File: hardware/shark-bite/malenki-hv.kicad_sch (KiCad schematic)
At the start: 18 parts, among them J1 Conn_01x02_Male-Connector, J2 Conn_01x08_Male, J3 Conn_01x02, U2 AP2204RA-3.3TRG1, U3 ATTiny1616-MNR

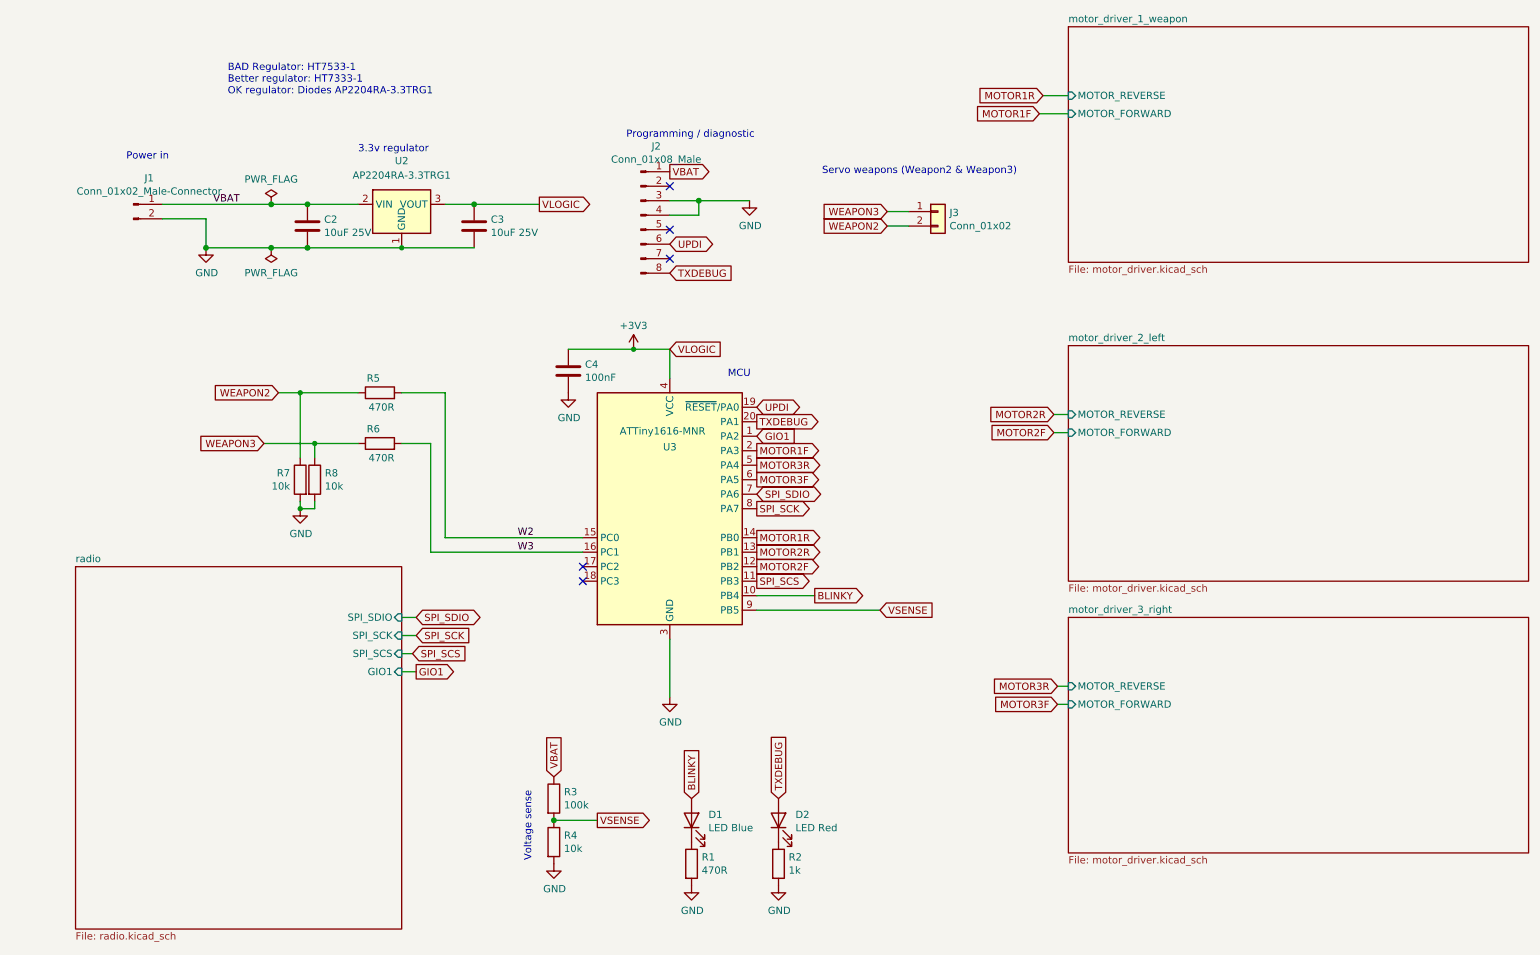
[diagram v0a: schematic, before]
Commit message: Added TVS Diodes
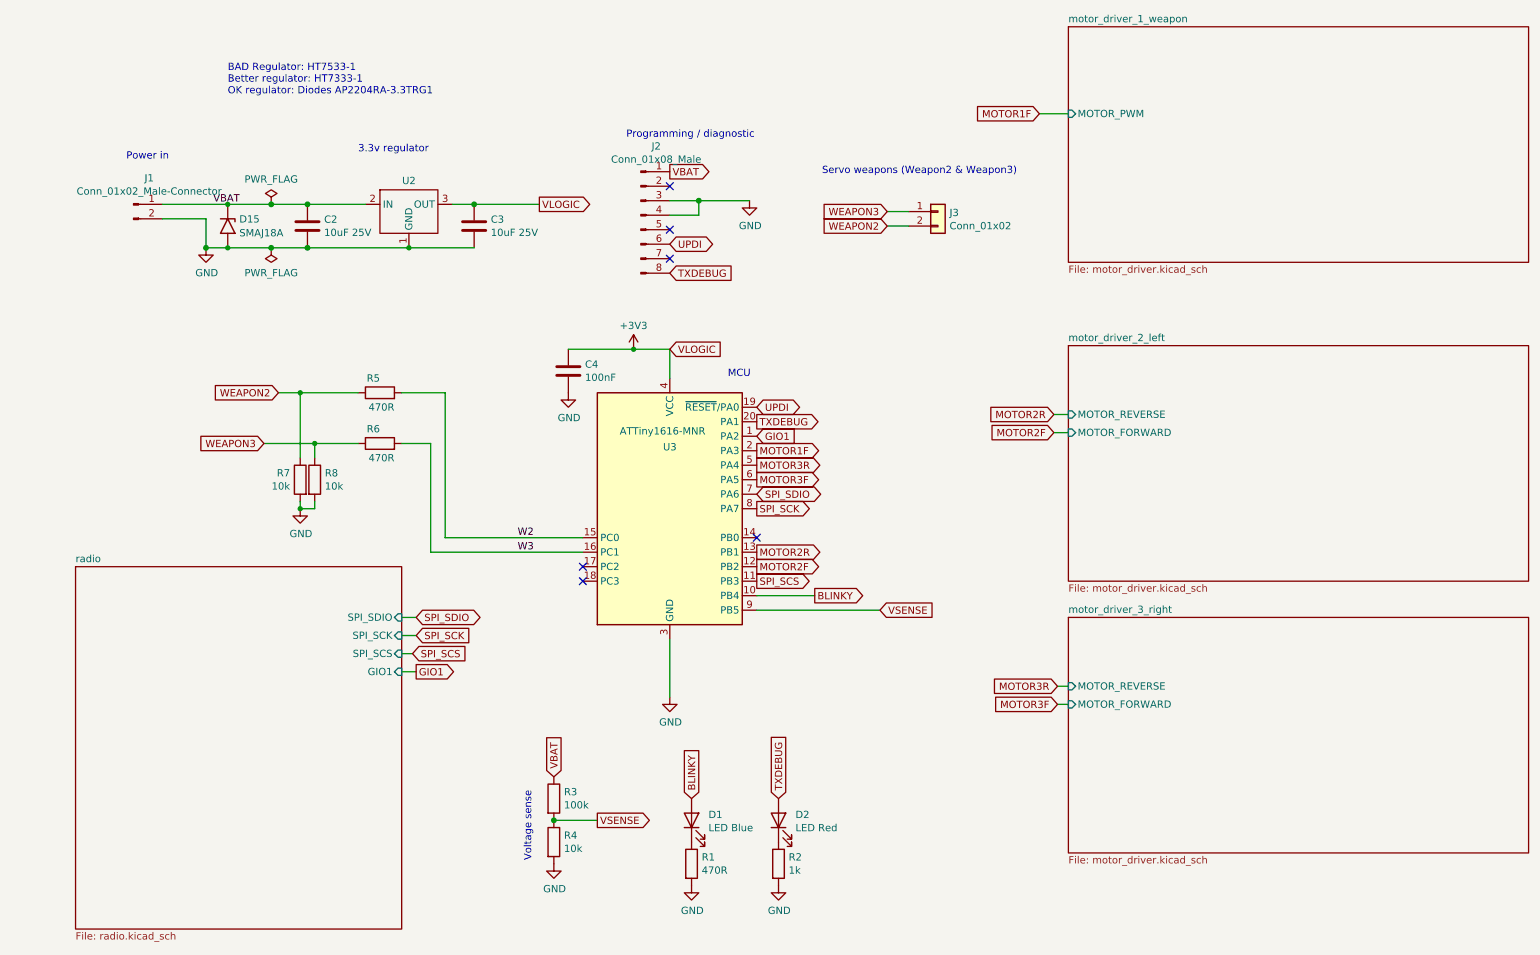
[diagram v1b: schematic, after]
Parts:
- removed U2: AP2204RA-3.3TRG1, Package_TO_SOT_SMD:SOT-89-3, symbol Regulator_Linear:HT75xx-1-SOT89
- added D15: SMAJ18A, Diode_SMD:D_SMA, symbol Diode:SMAJ18A
- added U2: ~, Package_TO_SOT_SMD:SOT-89-3, symbol Sharkbite:GATEMODE_GM7333
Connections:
- net +3V3: now also U2.3 (OUT)
- net GND: now also D15.2 (A2), U2.1 (GND)
- net VBAT: now also D15.1 (A1), U2.2 (IN)
- net MOTOR1R: no longer names the net of U3.14 (PB0)
- no-connect marks 5 -> 6
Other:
- sheet motor_driver_1_weapon ports: added MOTOR_PWM; removed MOTOR_FORWARD, MOTOR_REVERSE
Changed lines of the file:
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@@
   (junction (at 64.77 90.17) (diameter 0) (color 0 0 0 0)
   )
+  (junction (at 49.53 48.26) (diameter 0) (color 0 0 0 0)
+  )
   (junction (at 63.5 55.88) (diameter 1.016) (color 0 0 0 0)
   )
   (junction (at 92.71 48.26) (diameter 1.016) (color 0 0 0 0)
   )
+  (junction (at 81.28 55.88) (diameter 0) (color 0 0 0 0)
+  )
+  (junction (at 49.53 55.88) (diameter 0) (color 0 0 0 0)
+  )
   (junction (at 45.72 55.88) (diameter 1.016) (color 0 0 0 0)
   )
   (junction (at 62.23 81.28) (diameter 0) (color 0 0 0 0)
-  )
-  (junction (at 80.01 55.88) (diameter 0) (color 0 0 0 0)
   )
   (junction (at 57.15 48.26) (diameter 1.016) (color 0 0 0 0)
@@
   (no_connect (at 111.76 111.76))
   (no_connect (at 127 45.085))
+  (no_connect (at 142.24 106.68))
   (wire (pts (xy 165.1 52.07) (xy 168.91 52.07))
     (stroke (width 0) (type solid))
@@
     (stroke (width 0) (type default))
   )
-  (wire (pts (xy 38.1 48.26) (xy 57.15 48.26))
+  (wire (pts (xy 38.1 48.26) (xy 49.53 48.26))
+    (stroke (width 0) (type solid))
+  )
+  (wire (pts (xy 81.28 55.88) (xy 92.71 55.88))
     (stroke (width 0) (type solid))
   )
@@
     (stroke (width 0) (type solid))
   )
-  (wire (pts (xy 45.72 55.88) (xy 57.15 55.88))
+  (wire (pts (xy 45.72 55.88) (xy 49.53 55.88))
     (stroke (width 0) (type solid))
   )
@@
     (stroke (width 0) (type default))
   )
+  (wire (pts (xy 49.53 48.26) (xy 57.15 48.26))
+    (stroke (width 0) (type default))
+  )
   (wire (pts (xy 55.88 90.17) (xy 64.77 90.17))
     (stroke (width 0) (type default))
   )
-  (wire (pts (xy 80.01 55.88) (xy 92.71 55.88))
-    (stroke (width 0) (type solid))
-  )
   (wire (pts (xy 80.01 90.17) (xy 85.09 90.17))
     (stroke (width 0) (type default))
@@
     (stroke (width 0) (type default))
   )
-  (wire (pts (xy 63.5 55.88) (xy 80.01 55.88))
-    (stroke (width 0) (type solid))
-  )
   (wire (pts (xy 127 50.165) (xy 132.08 50.165))
     (stroke (width 0) (type solid))
@@
     (stroke (width 0) (type solid))
   )
-  (wire (pts (xy 63.5 48.26) (xy 72.39 48.26))
+  (wire (pts (xy 63.5 55.88) (xy 81.28 55.88))
+    (stroke (width 0) (type default))
+  )
+  (wire (pts (xy 63.5 48.26) (xy 73.66 48.26))
     (stroke (width 0) (type solid))
   )
@@
     (stroke (width 0) (type default))
   )
-  (wire (pts (xy 87.63 48.26) (xy 92.71 48.26))
-    (stroke (width 0) (type solid))
+  (wire (pts (xy 88.9 48.26) (xy 92.71 48.26))
+    (stroke (width 0) (type solid))
+  )
+  (wire (pts (xy 49.53 55.88) (xy 57.15 55.88))
+    (stroke (width 0) (type default))
   )
   (wire (pts (xy 62.23 81.28) (xy 62.23 92.71))
@@
   )
   (wire (pts (xy 165.1 49.53) (xy 168.91 49.53))
-    (stroke (width 0) (type solid))
-  )
-  (wire (pts (xy 192.405 29.21) (xy 196.85 29.21))
     (stroke (width 0) (type solid))
   )
@@
     (effects (font (size 1.27 1.27)) (justify right))
     (property "Intersheetrefs" "${INTERSHEET_REFS}" (at -53.34 -27.94 0)
-      (effects (font (size 1.27 1.27)) hide)
-    )
-  )
-  (global_label "MOTOR1R" (shape output) (at 142.24 106.68 0) (fields_autoplaced)
-    (effects (font (size 1.27 1.27)) (justify left))
-    (property "Intersheetrefs" "${INTERSHEET_REFS}" (at 154.0704 106.68 0)
-      (effects (font (size 1.27 1.27)) (justify left) hide)
-    )
-  )
-  (global_label "MOTOR1R" (shape input) (at 192.405 29.21 180)
-    (effects (font (size 1.27 1.27)) (justify right))
-    (property "Intersheetrefs" "${INTERSHEET_REFS}" (at 334.645 135.89 0)
       (effects (font (size 1.27 1.27)) hide)
     )
@@
         (path "/f41619e3-8cf2-4511-8a51-762d4de43197"
           (reference "D2") (unit 1)
+        )
+      )
+    )
+  )
+  (symbol (lib_id "Diode:SMAJ18A") (at 49.53 52.07 270) (unit 1)
+    (in_bom yes) (on_board yes) (dnp no) (fields_autoplaced)
+    (property "Reference" "D15" (at 51.562 50.8579 90)
+      (effects (font (size 1.27 1.27)) (justify left))
+    )
+    (property "Value" "SMAJ18A" (at 51.562 53.2821 90)
+      (effects (font (size 1.27 1.27)) (justify left))
+    )
+    (property "Footprint" "Diode_SMD:D_SMA" (at 44.45 52.07 0)
+      (effects (font (size 1.27 1.27)) hide)
+    )
+    (property "Datasheet" "https://www.littelfuse.com/media?resourcetype=datasheets&itemid=75e32973-b177-4ee3-a0ff-cedaf1abdb93&filename=smaj-datasheet" (at 49.53 50.8 0)
+      (effects (font (size 1.27 1.27)) hide)
+    )
+    (pin "1")
+    (pin "2")
+    (instances
+      (project "malenki-hv"
+        (path "/f41619e3-8cf2-4511-8a51-762d4de43197/b339fba4-a8e4-4c66-ad9c-610bd968ae93"
+          (reference "D15") (unit 1)
+        )
+        (path "/f41619e3-8cf2-4511-8a51-762d4de43197/159e78dd-19f3-45d1-a83d-5b1f96539c1f"
+          (reference "D16") (unit 1)
+        )
+        (path "/f41619e3-8cf2-4511-8a51-762d4de43197/ed035ea4-687d-4ec6-a6e6-057c20ae2a22"
+          (reference "D17") (unit 1)
+        )
+        (path "/f41619e3-8cf2-4511-8a51-762d4de43197"
+          (reference "D18") (unit 1)
         )
       )
@@
         (path "/f41619e3-8cf2-4511-8a51-762d4de43197"
           (reference "R6") (unit 1)
+        )
+      )
+    )
+  )
+  (symbol (lib_id "Sharkbite:GATEMODE_GM7333") (at 81.28 48.26 0) (unit 1)
+    (in_bom yes) (on_board yes) (dnp no) (fields_autoplaced)
+    (property "Reference" "U2" (at 81.28 44.1269 0)
+      (effects (font (size 1.27 1.27)))
+    )
+    (property "Value" "~" (at 80.01 45.72 0)
+      (effects (font (size 1.27 1.27)))
+    )
+    (property "Footprint" "Package_TO_SOT_SMD:SOT-89-3" (at 80.01 45.72 0)
+      (effects (font (size 1.27 1.27)) hide)
+    )
+    (property "Datasheet" "https://www.lcsc.com/datasheet/lcsc_datasheet_2308181508_GATEMODE-GM7333_C2833582.pdf" (at 80.01 45.72 0)
+      (effects (font (size 1.27 1.27)) hide)
+    )
+    (pin "1")
+    (pin "2")
+    (pin "3")
+    (instances
+      (project "malenki-hv"
+        (path "/f41619e3-8cf2-4511-8a51-762d4de43197"
+          (reference "U2") (unit 1)
         )
       )
@@
     )
   )
-  (symbol (lib_id "Regulator_Linear:HT75xx-1-SOT89") (at 80.01 50.8 0) (unit 1)
-    (in_bom yes) (on_board yes) (dnp no) (fields_autoplaced)
-    (property "Reference" "U2" (at 80.01 40.64 0)
-      (effects (font (size 1.27 1.27)))
-    )
-    (property "Value" "AP2204RA-3.3TRG1" (at 80.01 43.18 0)
-      (effects (font (size 1.27 1.27)))
-    )
-    (property "Footprint" "Package_TO_SOT_SMD:SOT-89-3" (at 80.01 42.545 0)
-      (effects (font (size 1.27 1.27) italic) hide)
-    )
-    (property "Datasheet" "" (at 80.01 48.26 0)
-      (effects (font (size 1.27 1.27)) hide)
-    )
-    (property "LCSC" "C151625" (at 80.01 50.8 0)
-      (effects (font (size 1.27 1.27)) hide)
-    )
-    (property "Manufacturer" "Diodes" (at 80.01 50.8 0)
-      (effects (font (size 1.27 1.27)) hide)
-    )
-    (pin "1")
-    (pin "2")
-    (pin "3")
-    (instances
-      (project "malenki-hv"
-        (path "/f41619e3-8cf2-4511-8a51-762d4de43197"
-          (reference "U2") (unit 1)
-        )
-      )
-    )
-  )
   (symbol (lib_id "malenki-nano-rescue:PWR_FLAG-power") (at 57.15 55.88 180) (unit 1)
     (in_bom yes) (on_board yes) (dnp no)
@@
       (effects (font (size 1.27 1.27)) (justify left top))
     )
-    (pin "MOTOR_REVERSE" input (at 196.85 29.21 180)
-      (effects (font (size 1.27 1.27)) (justify left))
-    )
-    (pin "MOTOR_FORWARD" input (at 196.85 32.385 180)
-      (effects (font (size 1.27 1.27)) (justify left))
-    )
+    (pin "MOTOR_PWM" input (at 196.85 32.385 180)
+      (effects (font (size 1.27 1.27)) (justify left))
+    )

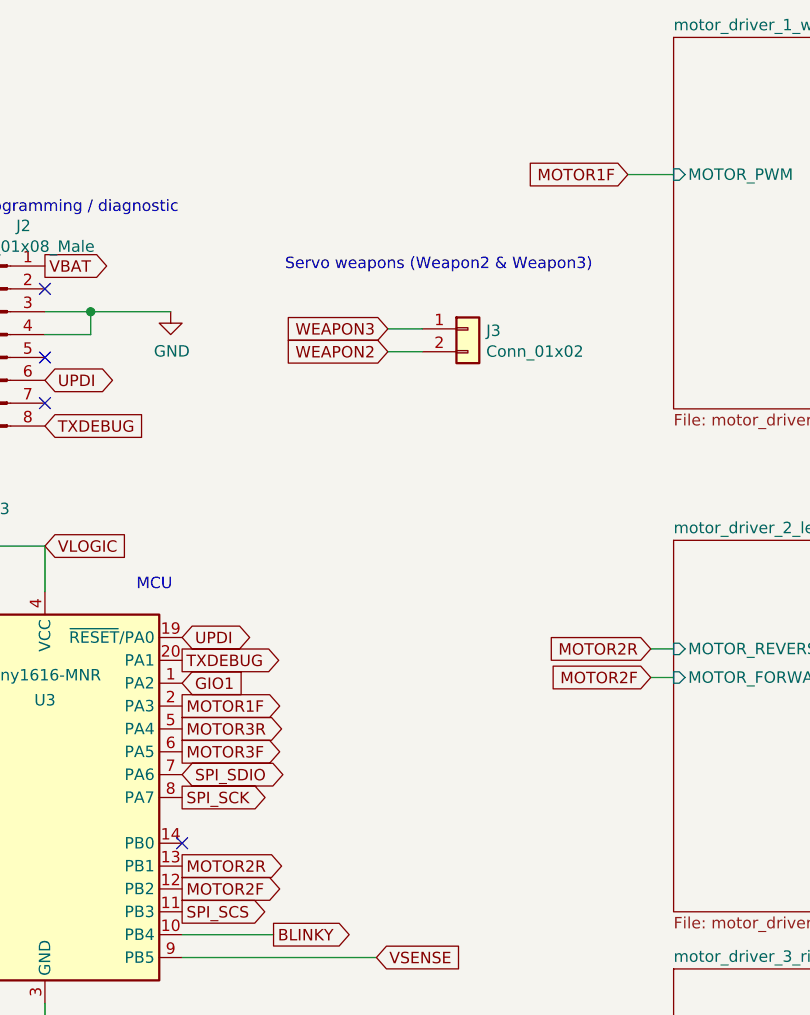
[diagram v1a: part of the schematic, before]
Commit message: Removed Extra Diodes
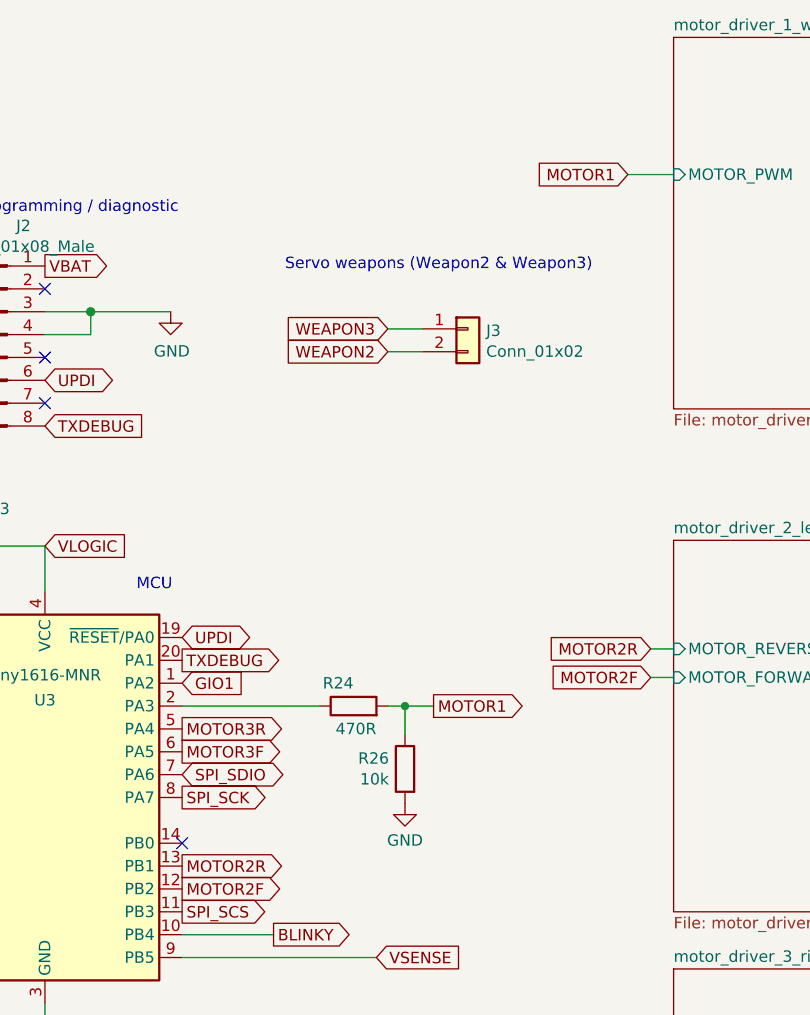
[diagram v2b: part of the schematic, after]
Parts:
- added R24: 470R, Resistor_SMD:R_0402_1005Metric, symbol malenki-nano-rescue:R-Device
- added R26: 10k, Resistor_SMD:R_0402_1005Metric, symbol malenki-nano-rescue:R-Device
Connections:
- net GND: now also R26.2
- net MOTOR1F: no longer names the net of U3.2 (PA3)
- net MOTOR1F: now also R24.1
- new net MOTOR1: R24.2, R26.1
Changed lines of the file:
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@@
   (junction (at 45.72 55.88) (diameter 1.016) (color 0 0 0 0)
+  )
+  (junction (at 167.005 91.44) (diameter 0) (color 0 0 0 0)
   )
   (junction (at 62.23 81.28) (diameter 0) (color 0 0 0 0)
@@
     (stroke (width 0) (type default))
   )
+  (wire (pts (xy 167.005 91.44) (xy 170.18 91.44))
+    (stroke (width 0) (type default))
+  )
   (wire (pts (xy 49.53 48.26) (xy 57.15 48.26))
     (stroke (width 0) (type default))
   )
+  (wire (pts (xy 165.1 91.44) (xy 167.005 91.44))
+    (stroke (width 0) (type default))
+  )
   (wire (pts (xy 55.88 90.17) (xy 64.77 90.17))
     (stroke (width 0) (type default))
@@
     (stroke (width 0) (type solid))
   )
+  (wire (pts (xy 142.24 91.44) (xy 157.48 91.44))
+    (stroke (width 0) (type default))
+  )
   (wire (pts (xy 120.65 73.66) (xy 109.22 73.66))
     (stroke (width 0) (type solid))
@@
   (wire (pts (xy 92.71 48.26) (xy 104.14 48.26))
     (stroke (width 0) (type solid))
+  )
+  (wire (pts (xy 167.005 91.44) (xy 167.005 94.615))
+    (stroke (width 0) (type default))
   )
   (text "Voltage sense" (at 102.87 151.13 90)
@@
     (effects (font (size 1.27 1.27)) (justify left bottom))
   )
-  (global_label "MOTOR1F" (shape output) (at 142.24 91.44 0) (fields_autoplaced)
-    (effects (font (size 1.27 1.27)) (justify left))
-    (property "Intersheetrefs" "${INTERSHEET_REFS}" (at 153.889 91.44 0)
+  (global_label "MOTOR1" (shape output) (at 170.18 91.44 0) (fields_autoplaced)
+    (effects (font (size 1.27 1.27)) (justify left))
+    (property "Intersheetrefs" "${INTERSHEET_REFS}" (at 180.8198 91.44 0)
       (effects (font (size 1.27 1.27)) (justify left) hide)
     )
@@
     )
   )
-  (global_label "MOTOR1F" (shape input) (at 191.77 32.385 180)
+  (global_label "MOTOR1" (shape input) (at 191.77 32.385 180)
     (effects (font (size 1.27 1.27)) (justify right))
     (property "Intersheetrefs" "${INTERSHEET_REFS}" (at 334.01 123.825 0)
@@
     )
   )
+  (symbol (lib_id "malenki-nano-rescue:R-Device") (at 167.005 98.425 0) (mirror y) (unit 1)
+    (in_bom yes) (on_board yes) (dnp no)
+    (property "Reference" "R26" (at 165.227 97.2566 0)
+      (effects (font (size 1.27 1.27)) (justify left))
+    )
+    (property "Value" "10k" (at 165.227 99.568 0)
+      (effects (font (size 1.27 1.27)) (justify left))
+    )
+    (property "Footprint" "Resistor_SMD:R_0402_1005Metric" (at 168.783 98.425 90)
+      (effects (font (size 1.27 1.27)) hide)
+    )
+    (property "Datasheet" "~" (at 167.005 98.425 0)
+      (effects (font (size 1.27 1.27)) hide)
+    )
+    (property "Partnum" "C25804" (at 167.005 98.425 0)
+      (effects (font (size 1.27 1.27)) hide)
+    )
+    (property "LCSC" "C25744" (at 167.005 98.425 0)
+      (effects (font (size 1.27 1.27)) hide)
+    )
+    (property "Manufacturer" "Uniroyal" (at 167.005 98.425 0)
+      (effects (font (size 1.27 1.27)) hide)
+    )
+    (pin "1")
+    (pin "2")
+    (instances
+      (project "malenki-hv"
+        (path "/f41619e3-8cf2-4511-8a51-762d4de43197"
+          (reference "R26") (unit 1)
+        )
+      )
+    )
+  )
+  (symbol (lib_id "power:GND") (at 167.005 102.235 0) (unit 1)
+    (in_bom yes) (on_board yes) (dnp no) (fields_autoplaced)
+    (property "Reference" "#PWR070" (at 167.005 108.585 0)
+      (effects (font (size 1.27 1.27)) hide)
+    )
+    (property "Value" "GND" (at 167.005 106.3681 0)
+      (effects (font (size 1.27 1.27)))
+    )
+    (property "Footprint" "" (at 167.005 102.235 0)
+      (effects (font (size 1.27 1.27)) hide)
+    )
+    (property "Datasheet" "" (at 167.005 102.235 0)
+      (effects (font (size 1.27 1.27)) hide)
+    )
+    (pin "1")
+    (instances
+      (project "malenki-hv"
+        (path "/f41619e3-8cf2-4511-8a51-762d4de43197"
+          (reference "#PWR070") (unit 1)
+        )
+      )
+    )
+  )
   (symbol (lib_id "malenki-nano-rescue:GND-power") (at 127 134.62 0) (unit 1)
     (in_bom yes) (on_board yes) (dnp no)
@@
         )
       )
+    )
+  )
+  (symbol (lib_id "malenki-nano-rescue:R-Device") (at 161.29 91.44 90) (unit 1)
+    (in_bom yes) (on_board yes) (dnp no)
+    (property "Reference" "R24" (at 161.29 88.9 90)
+      (effects (font (size 1.27 1.27)) (justify left))
+    )
+    (property "Value" "470R" (at 163.83 93.98 90)
+      (effects (font (size 1.27 1.27)) (justify left))
+    )
+    (property "Footprint" "Resistor_SMD:R_0402_1005Metric" (at 161.29 93.218 90)
+      (effects (font (size 1.27 1.27)) hide)
+    )
+    (property "Datasheet" "~" (at 161.29 91.44 0)
+      (effects (font (size 1.27 1.27)) hide)
+    )
+    (property "Partnum" "" (at 161.29 91.44 0)
+      (effects (font (size 1.27 1.27)) hide)
+    )
+    (property "LCSC" "C25117" (at 161.29 91.44 0)
+      (effects (font (size 1.27 1.27)) hide)
+    )
+    (pin "1")
+    (pin "2")
+    (instances
+      (project "malenki-hv"
+        (path "/f41619e3-8cf2-4511-8a51-762d4de43197"
+          (reference "R24") (unit 1)
+        )
+      )
